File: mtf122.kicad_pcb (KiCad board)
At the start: 2 copper layers, 500 x 194 mm, 192 parts, among them J1 CONN_CAP_IBM_F, SW1 1,8, SW10 A,8, SW100 6,2, SW101 7,2, SW102 7,1, SW103 8,2, SW104 9,1, SW105 A,1, SW106 A,2, SW107 B,2, SW108 C,2, SW109 D,2, SW11 B,8, SW110 D,3, SW111 E,3, SW112 E,2, SW113 F,3, SW114 G,3, SW115 G,2, SW116 1,1, SW117 2,1, SW118 3,1, SW119 4,1, SW12 C,8, SW120 6,1, SW121 8,1, SW122 C,1, SW123 D,1, SW124 E,1, SW125 F,1, SW126 F,2, SW127 G,1, SW13 1,7, SW14 2,7, SW15 3,7, SW16 4,7, SW17 5,7, SW18 6,7, SW19 7,7, SW2 2,8, SW20 8,7, SW21 9,7, SW22 A,7, SW23 B,7, SW24 C,7, SW25 1,5, SW26 1,6, SW27 2,6, SW28 3,6, SW29 4,6, SW3 3,8, SW30 5,6, SW31 5,5, SW32 6,6, SW33 7,6, SW34 8,5, SW35 8,6, SW36 9,6, SW37 9,5, SW38 A,6, SW39 B,6, SW4 4,8, SW40 C,6, SW41 D,7, SW42 D,8, SW43 E,7, SW44 E,8, SW45 F,7, SW46 F,8, SW47 G,7, SW48 G,8, SW49 1,4, SW5 5,8, SW50 2,4, SW51 2,5, SW52 3,5, SW53 4,5, SW54 5,4, SW55 6,5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

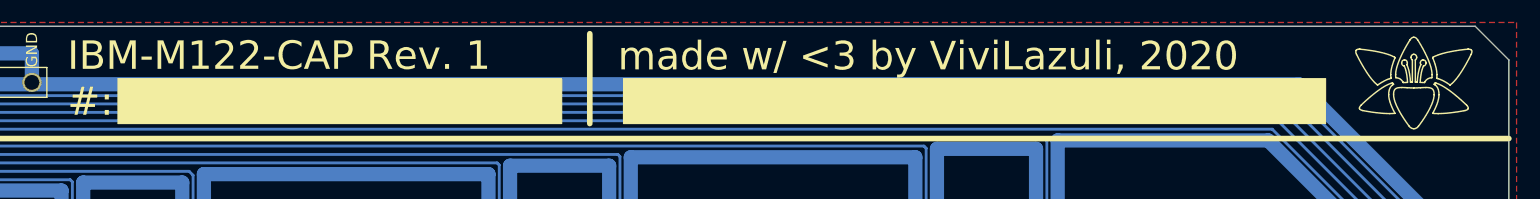
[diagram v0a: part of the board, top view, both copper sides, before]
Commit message: Removed drawings from back and front silkscreen
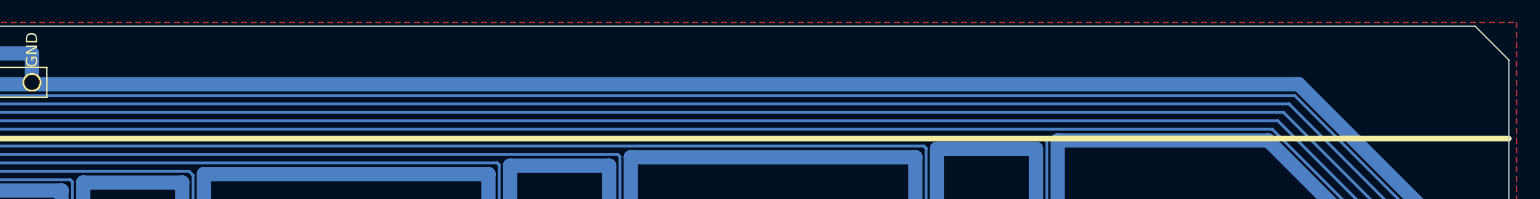
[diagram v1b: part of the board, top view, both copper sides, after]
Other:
- board text removed: "IBM-M122-CAP Rev. 1 #:"
- board text removed: "made w/ <3 by ViviLazuli, 2020"

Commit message: Updated the PCB edge lines with the old style M122 barrel plate design
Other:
- board size 500 x 194 mm -> 500.1 x 184 mm

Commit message: Changed the controller pins location and rerouted the connections on B.Cu
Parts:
- moved J1 311.5 mm to (419.0, 164.1)
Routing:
- net COL_1: track 257.3 -> 769.2 mm
- net COL_2: track 240.5 -> 744.3 mm
- net COL_3: track 205.4 -> 698.5 mm
- net COL_4: track 239.0 -> 688.1 mm
- net COL_5: track 208.0 -> 636.4 mm
- net COL_6: track 275.5 -> 650.2 mm
- net COL_7: track 240.4 -> 594.5 mm
- net COL_8: track 325.0 -> 625.3 mm
- net COL_G: track 493.9 -> 207.9 mm
- net COL_9: track 266.5 -> 546.2 mm
- net COL_F: track 466.5 -> 234.7 mm
- net COL_A: track 298.0 -> 524.0 mm
- net COL_B: track 308.5 -> 513.5 mm
- net COL_C: track 345.5 -> 500.6 mm
- net COL_E: track 440.9 -> 302.5 mm
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
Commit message: Changed the controller pins location and rerouted the connections on the F.Cu
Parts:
- moved J1 3.24 mm to (418.6, 160.9)
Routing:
- net ROW_4: track 858.1 -> 1206.4 mm
- net ROW_8: track 686.1 -> 1034.3 mm
- net ROW_3: track 850.3 -> 1197.9 mm
- net ROW_7: track 661.6 -> 1008.6 mm
- net ROW_2: track 897.6 -> 1243.7 mm
- net ROW_1: track 882.4 -> 1227.0 mm
- net ROW_5: track 796.4 -> 1140.4 mm
- net ROW_6: track 751.6 -> 1095.2 mm
- net GND: track 9722.3 -> 9614.0 mm
- net COL_F: track 234.7 -> 236.4 mm
- net COL_G: track 207.9 -> 209.6 mm
- net COL_C: track 500.6 -> 502.3 mm
- net COL_B: track 513.5 -> 515.2 mm
- net COL_A: track 524.0 -> 525.8 mm
- net COL_7: track 594.5 -> 596.3 mm
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- removed copper zone on F.Cu, net GND
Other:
- board size 500.1 x 184 mm -> 500 x 184 mm

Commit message: Changed the PCB edges and rerouter the row connections
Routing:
- net GND: track 9614.0 -> 9571.0 mm
- net ROW_7: track 1008.6 -> 1050.4 mm
- net ROW_8: track 1034.3 -> 1075.0 mm
- net ROW_6: track 1095.2 -> 1126.6 mm
- net ROW_5: track 1140.4 -> 1171.8 mm
- net ROW_4: track 1206.4 -> 1237.8 mm
- net ROW_3: track 1197.9 -> 1229.3 mm
- net ROW_2: track 1243.7 -> 1274.9 mm
- net ROW_1: track 1227.0 -> 1258.2 mm
- net COL_C: track 502.3 -> 486.0 mm
- net COL_B: track 515.2 -> 499.0 mm
- net COL_A: track 525.8 -> 509.6 mm
- net COL_9: track 547.9 -> 531.8 mm
- net COL_8: track 627.0 -> 610.9 mm
- net COL_7: track 596.3 -> 580.2 mm
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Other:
- board size 500 x 184 mm -> 500 x 194 mm

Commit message: Added Copper fill areas
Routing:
- net GND: track 9571.0 -> 9403.0 mm
- net COL_1: track 755.1 -> 611.5 mm
- net COL_2: track 730.1 -> 593.0 mm
- net COL_4: track 673.9 -> 549.7 mm
- net COL_3: track 684.3 -> 560.9 mm
- net COL_5: track 622.1 -> 504.4 mm
- net COL_6: track 635.9 -> 524.6 mm
- net COL_7: track 580.2 -> 475.3 mm
- net COL_8: track 610.9 -> 512.5 mm
- net COL_9: track 531.8 -> 439.8 mm
- net COL_A: track 509.6 -> 424.0 mm
- net COL_B: track 499.0 -> 419.9 mm
- net COL_C: track 486.0 -> 413.6 mm
- net COL_D: track 335.9 -> 264.0 mm
- net COL_E: track 304.2 -> 238.7 mm
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- added copper zone on B.Cu, net GND
- added copper zone on F.Cu, net GND

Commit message: Added an extra copper fill area and resized the others
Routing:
- net GND: track 9403.0 -> 9439.6 mm

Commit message: Removed unnecessary solder mask
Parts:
- moved J1 1.80 mm to (419.6, 162.4)
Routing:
- net GND: track 9439.6 -> 9430.5 mm
- net COL_G: track 188.6 -> 183.9 mm
- net ROW_4: track 1237.8 -> 1238.9 mm
- net ROW_6: track 1126.6 -> 1127.5 mm
- net ROW_5: track 1171.8 -> 1172.7 mm
- net ROW_2: track 1274.9 -> 1275.8 mm
